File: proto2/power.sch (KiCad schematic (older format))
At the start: 24 parts, among them U13 LDO

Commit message: Fixing the issues the filter-fix merge created.
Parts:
- PS1: symbol BCR:CUI_PDQE20_ISOLATED_DCDC -> proto2-rescue:CUI_PDQE20_ISOLATED_DCDC-BCR
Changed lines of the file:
@@
 Raspberry Pi draws 1.3A and recomends 2.5A @ 5V.\nBeagleBone draws 1.2A and recomends at least 2A.
 $Comp
-L BCR:CUI_PDQE20_ISOLATED_DCDC PS1
+L proto2-rescue:CUI_PDQE20_ISOLATED_DCDC-BCR PS1
 U 1 1 61BF7DE1
 P 4050 2000
+AR Path="/61BF7DE1" Ref="PS1"  Part="1"
+AR Path="/619EB672/61BF7DE1" Ref="PS1"  Part="1"
 F 0 "PS1" H 4050 2425 50  0000 C CNN
 F 1 "CUI_PDQE20_ISOLATED_DCDC" H 4050 2334 50  0000 C CNN

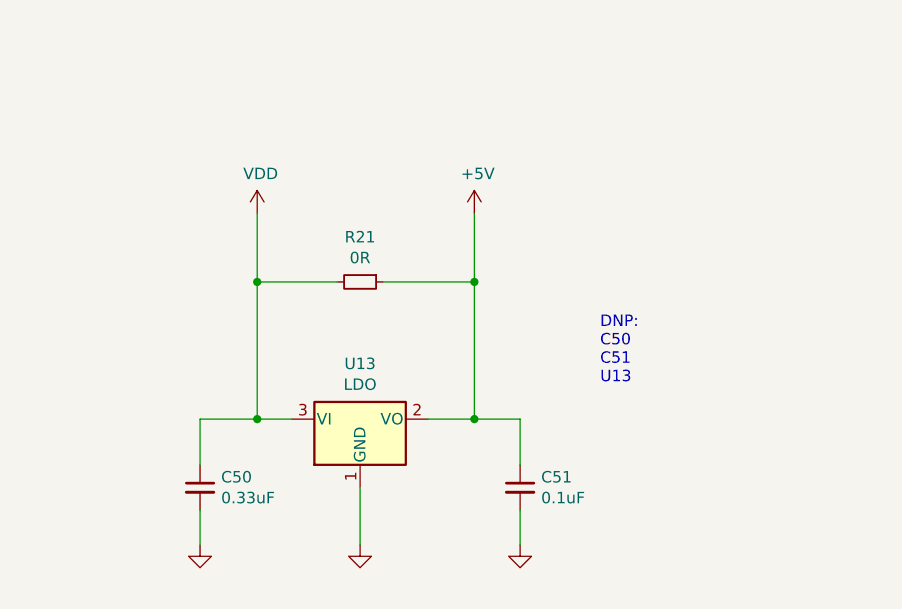
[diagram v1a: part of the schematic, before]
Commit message: Replaced LDO with a D2PAK type. Cleaned some traces.
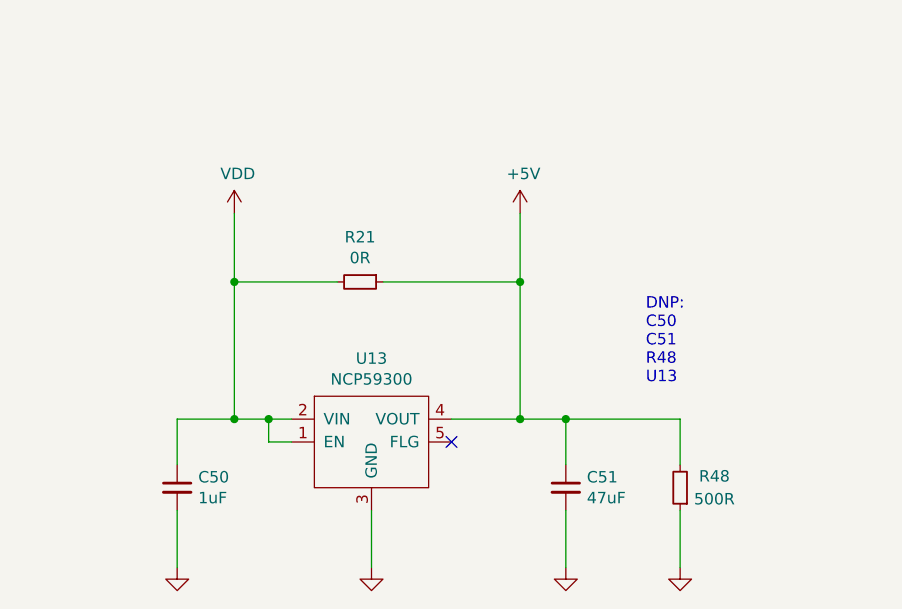
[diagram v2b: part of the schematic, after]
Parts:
- removed U13: LDO, JLCPCB:TO-252-2, symbol Regulator_Linear:AP1117-50
- added R48: 500R, Capacitor_SMD:C_0805_2012Metric, symbol Device:R_Small
- added U13: NCP59300, Package_TO_SOT_SMD:TO-263-5_TabPin3, symbol BCR:NCP59300
- C50: value 0.33uF -> 1uF; LCSC C1740 -> (none)
- C51: value 0.1uF -> 47uF; LCSC C49678 -> (none)
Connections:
- net +5V: now also R48.2, U13.4 (VOUT)
- net GND: now also R48.1, U13.3 (GND)
- net VDD: now also U13.1 (EN), U13.2 (VIN)
- no-connect marks 0 -> 1
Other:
- note added: "DNP:\nC50\nC51\nR48\nU13"
- note removed: "DNP:\nC50\nC51\nU13"
- moved on the sheet: C50, C51
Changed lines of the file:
@@
 Comment4 ""
 $EndDescr
-$Comp
-L Regulator_Linear:AP1117-50 U13
-U 1 1 61B47373
-P 3900 5500
-F 0 "U13" H 3900 5742 50  0000 C CNN
-F 1 "LDO" H 3900 5651 50  0000 C CNN
-F 2 "JLCPCB:TO-252-2" H 3900 5700 50  0001 C CNN
-F 3 "http://www.diodes.com/datasheets/AP1117.pdf" H 4000 5250 50  0001 C CNN
-F 4 "C58069" H 3900 5500 50  0001 C CNN "LCSC"
-	1    3900 5500
-	1    0    0    -1
-$EndComp
-Wire Wire Line
-	3900 5800 3900 6050
-Wire Wire Line
-	4200 5500 4400 5500
-Wire Wire Line
-	4400 5500 4400 4900
-Wire Wire Line
-	3600 5500 3450 5500
+Wire Wire Line
+	3950 5900 3950 6150
+Wire Wire Line
+	4300 5500 4600 5500
+Wire Wire Line
+	4600 5500 4600 4900
+Wire Wire Line
+	3600 5500 3500 5500
 Wire Wire Line
 	900  2200 900  2450
@@
 $EndComp
 Wire Wire Line
-	3450 5500 3450 4900
+	3350 5500 3350 4900
 $Comp
 L power:VDD #PWR0108
@@
 L power:VDD #PWR0109
 U 1 1 620C752B
-P 3450 4600
-F 0 "#PWR0109" H 3450 4450 50  0001 C CNN
-F 1 "VDD" H 3465 4773 50  0000 C CNN
-F 2 "" H 3450 4600 50  0001 C CNN
-F 3 "" H 3450 4600 50  0001 C CNN
-	1    3450 4600
+P 3350 4600
+F 0 "#PWR0109" H 3350 4450 50  0001 C CNN
+F 1 "VDD" H 3365 4773 50  0000 C CNN
+F 2 "" H 3350 4600 50  0001 C CNN
+F 3 "" H 3350 4600 50  0001 C CNN
+	1    3350 4600
 	1    0    0    -1
 $EndComp
@@
 L power:GND #PWR0112
 U 1 1 620C8052
-P 3900 6050
-F 0 "#PWR0112" H 3900 5800 50  0001 C CNN
-F 1 "GND" H 3905 5877 50  0001 C CNN
-F 2 "" H 3900 6050 50  0001 C CNN
-F 3 "" H 3900 6050 50  0001 C CNN
-	1    3900 6050
+P 3950 6150
+F 0 "#PWR0112" H 3950 5900 50  0001 C CNN
+F 1 "GND" H 3955 5977 50  0001 C CNN
+F 2 "" H 3950 6150 50  0001 C CNN
+F 3 "" H 3950 6150 50  0001 C CNN
+	1    3950 6150
 	1    0    0    -1
 $EndComp
@@
 $EndComp
 Wire Wire Line
-	3800 4900 3450 4900
-Connection ~ 3450 4900
-Wire Wire Line
-	3450 4900 3450 4600
-Wire Wire Line
-	4000 4900 4400 4900
-Connection ~ 4400 4900
-Wire Wire Line
-	4400 4900 4400 4600
+	3800 4900 3350 4900
+Connection ~ 3350 4900
+Wire Wire Line
+	3350 4900 3350 4600
+Wire Wire Line
+	4000 4900 4600 4900
+Connection ~ 4600 4900
+Wire Wire Line
+	4600 4900 4600 4600
 $Comp
 L Device:C_Small C50
 U 1 1 61BCD4E8
-P 3200 5800
-F 0 "C50" H 3292 5846 50  0000 L CNN
-F 1 "0.33uF" H 3292 5755 50  0000 L CNN
-F 2 "Capacitor_SMD:C_0805_2012Metric" H 3200 5800 50  0001 C CNN
-F 3 "~" H 3200 5800 50  0001 C CNN
-F 4 "C1740" H 3200 5800 50  0001 C CNN "LCSC"
-	1    3200 5800
+P 3100 5800
+F 0 "C50" H 3192 5846 50  0000 L CNN
+F 1 "1uF" H 3192 5755 50  0000 L CNN
+F 2 "Capacitor_SMD:C_0805_2012Metric" H 3100 5800 50  0001 C CNN
+F 3 "~" H 3100 5800 50  0001 C CNN
+F 4 "" H 3100 5800 50  0001 C CNN "LCSC"
+	1    3100 5800
 	1    0    0    -1
 $EndComp
@@
 L Device:C_Small C51
 U 1 1 61BCDFDB
-P 4600 5800
-F 0 "C51" H 4692 5846 50  0000 L CNN
-F 1 "0.1uF" H 4692 5755 50  0000 L CNN
-F 2 "Capacitor_SMD:C_0805_2012Metric" H 4600 5800 50  0001 C CNN
-F 3 "~" H 4600 5800 50  0001 C CNN
-F 4 "C49678" H 4600 5800 50  0001 C CNN "LCSC"
-	1    4600 5800
-	1    0    0    -1
-$EndComp
-Wire Wire Line
-	4400 5500 4600 5500
-Wire Wire Line
-	4600 5500 4600 5700
-Connection ~ 4400 5500
-Wire Wire Line
-	3450 5500 3200 5500
-Wire Wire Line
-	3200 5500 3200 5700
-Connection ~ 3450 5500
+P 4800 5800
+F 0 "C51" H 4892 5846 50  0000 L CNN
+F 1 "47uF" H 4892 5755 50  0000 L CNN
+F 2 "Capacitor_SMD:C_0805_2012Metric" H 4800 5800 50  0001 C CNN
+F 3 "~" H 4800 5800 50  0001 C CNN
+F 4 "" H 4800 5800 50  0001 C CNN "LCSC"
+	1    4800 5800
+	1    0    0    -1
+$EndComp
+Wire Wire Line
+	4600 5500 4800 5500
+Wire Wire Line
+	4800 5500 4800 5700
+Connection ~ 4600 5500
+Wire Wire Line
+	3350 5500 3100 5500
+Wire Wire Line
+	3100 5500 3100 5700
+Connection ~ 3350 5500
 $Comp
 L power:GND #PWR0122
 U 1 1 61BCFCA7
-P 3200 6050
-F 0 "#PWR0122" H 3200 5800 50  0001 C CNN
-F 1 "GND" H 3205 5877 50  0001 C CNN
-F 2 "" H 3200 6050 50  0001 C CNN
-F 3 "" H 3200 6050 50  0001 C CNN
-	1    3200 6050
+P 3100 6150
+F 0 "#PWR0122" H 3100 5900 50  0001 C CNN
+F 1 "GND" H 3105 5977 50  0001 C CNN
+F 2 "" H 3100 6150 50  0001 C CNN
+F 3 "" H 3100 6150 50  0001 C CNN
+	1    3100 6150
 	1    0    0    -1
 $EndComp
@@
 L power:GND #PWR0123
 U 1 1 61BCFF8F
-P 4600 6050
-F 0 "#PWR0123" H 4600 5800 50  0001 C CNN
-F 1 "GND" H 4605 5877 50  0001 C CNN
-F 2 "" H 4600 6050 50  0001 C CNN
-F 3 "" H 4600 6050 50  0001 C CNN
-	1    4600 6050
-	1    0    0    -1
-$EndComp
-Wire Wire Line
-	4600 6050 4600 5900
-Wire Wire Line
-	3200 6050 3200 5900
+P 4800 6150
+F 0 "#PWR0123" H 4800 5900 50  0001 C CNN
+F 1 "GND" H 4805 5977 50  0001 C CNN
+F 2 "" H 4800 6150 50  0001 C CNN
+F 3 "" H 4800 6150 50  0001 C CNN
+	1    4800 6150
+	1    0    0    -1
+$EndComp
+Wire Wire Line
+	4800 6150 4800 5900
+Wire Wire Line
+	3100 6150 3100 5900
 Wire Wire Line
 	1350 1900 1350 1800
@@
 Text Notes 9700 4750 0    50   ~ 0
 DNP:\nC52\nC53\nR18
-Text Notes 4950 5350 0    50   ~ 0
-DNP:\nC50\nC51\nU13
+Text Notes 5150 5350 0    50   ~ 0
+DNP:\nC50\nC51\nR48\nU13
 Text Notes 9150 2150 0    50   ~ 0
 DNP:\nR19\nR20
@@
 L power:+5V #PWR0104
 U 1 1 61DA9C72
-P 4400 4600
-F 0 "#PWR0104" H 4400 4450 50  0001 C CNN
-F 1 "+5V" H 4415 4773 50  0000 C CNN
-F 2 "" H 4400 4600 50  0001 C CNN
-F 3 "" H 4400 4600 50  0001 C CNN
-	1    4400 4600
+P 4600 4600
+F 0 "#PWR0104" H 4600 4450 50  0001 C CNN
+F 1 "+5V" H 4615 4773 50  0000 C CNN
+F 2 "" H 4600 4600 50  0001 C CNN
+F 3 "" H 4600 4600 50  0001 C CNN
+	1    4600 4600
 	1    0    0    -1
 $EndComp
@@
 	1    0    0    -1
 $EndComp
+$Comp
+L BCR:NCP59300 U13
+U 1 1 61CAD4D2
+P 3950 5800
+F 0 "U13" H 3950 6365 50  0000 C CNN
+F 1 "NCP59300" H 3950 6274 50  0000 C CNN
+F 2 "Package_TO_SOT_SMD:TO-263-5_TabPin3" H 3950 5800 50  0001 C CNN
+F 3 "https://www.onsemi.com/pdf/datasheet/ncp59300-d.pdf" H 3950 5800 50  0001 C CNN
+	1    3950 5800
+	1    0    0    -1
+$EndComp
+Wire Wire Line
+	3600 5600 3500 5600
+Wire Wire Line
+	3500 5600 3500 5500
+Connection ~ 3500 5500
+Wire Wire Line
+	3500 5500 3350 5500
+NoConn ~ 4300 5600
+$Comp
+L Device:R_Small R48
+U 1 1 61CC0990
+P 5300 5800
+F 0 "R48" H 5150 5750 50  0000 C CNN
+F 1 "500R" H 5150 5850 50  0000 C CNN
+F 2 "Capacitor_SMD:C_0805_2012Metric" H 5300 5800 50  0001 C CNN
+F 3 "~" H 5300 5800 50  0001 C CNN
+F 4 "C17888" H 5300 5800 50  0001 C CNN "LCSC"
+	1    5300 5800
+	-1   0    0    1
+$EndComp
+Wire Wire Line
+	5300 5700 5300 5500
+Wire Wire Line
+	5300 5500 4800 5500
+Connection ~ 4800 5500
+Wire Wire Line
+	5300 5900 5300 6150
+$Comp
+L power:GND #PWR013
+U 1 1 61CC641D
+P 5300 6150
+F 0 "#PWR013" H 5300 5900 50  0001 C CNN
+F 1 "GND" H 5305 5977 50  0001 C CNN
+F 2 "" H 5300 6150 50  0001 C CNN
+F 3 "" H 5300 6150 50  0001 C CNN
+	1    5300 6150
+	1    0    0    -1
+$EndComp

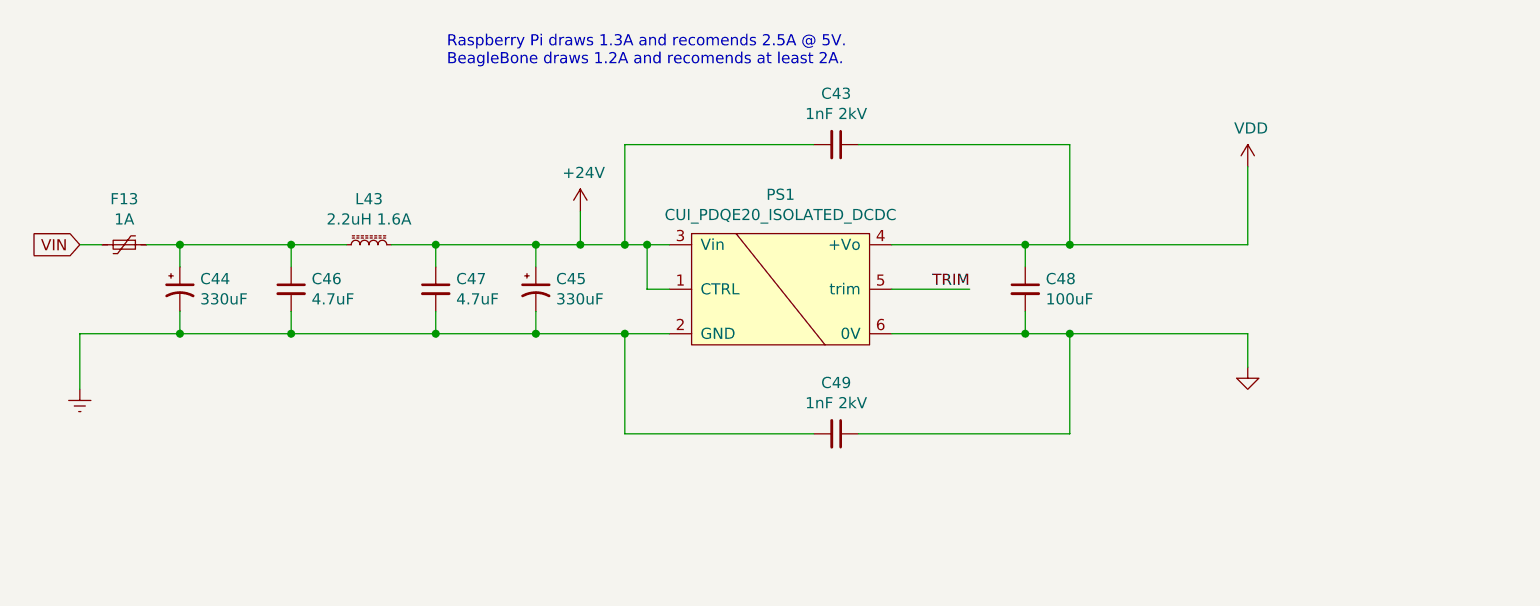
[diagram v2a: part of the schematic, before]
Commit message: Added reverse polarity diode.
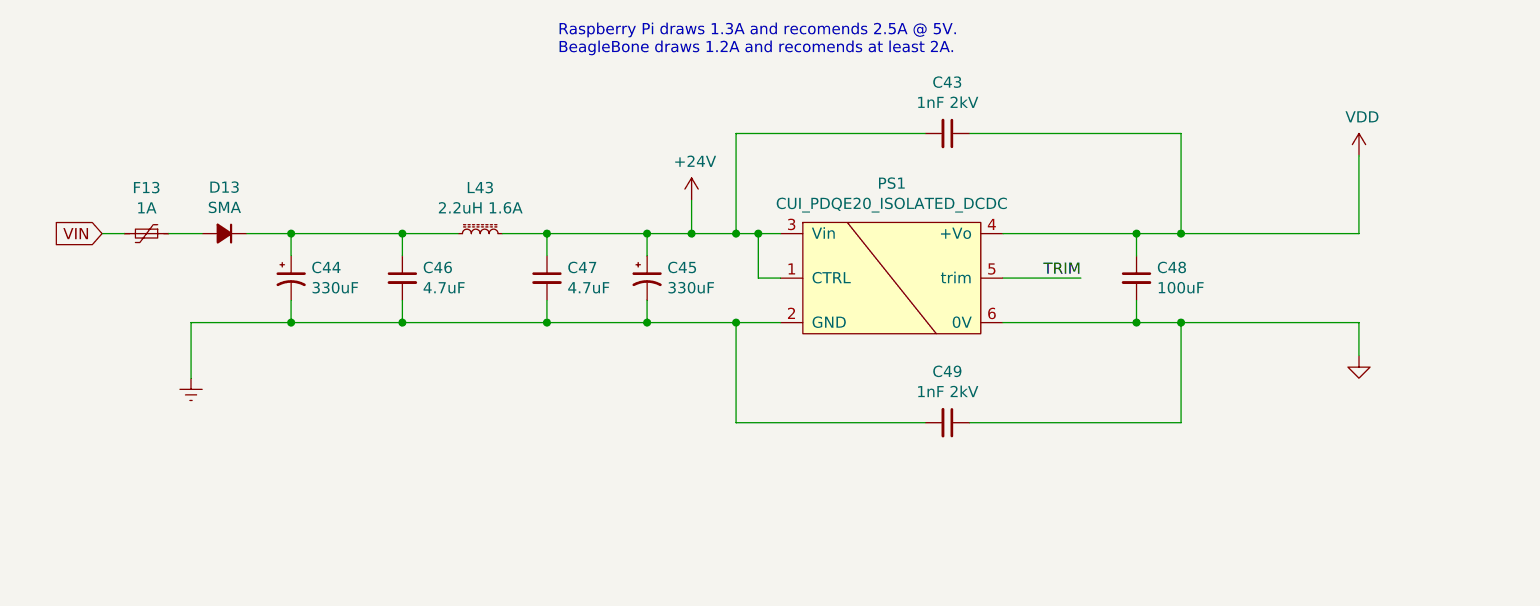
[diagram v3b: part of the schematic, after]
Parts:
- added D13: SMA, Diode_SMD:D_SOD-123F, symbol Device:D_Small_ALT
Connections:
- net at C44.1, C46.1, L43.1: now also D13.1 (K); no longer F13.1
- new net: D13.2 (A), F13.1
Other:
- moved on the sheet: C43, C44, C45, C46, C47, C48, C49, F13, L43, PS1

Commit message: Updates and changes for production run of 0.1.0
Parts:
- C52, C53: LCSC C49678 -> (none)
- R18: LCSC C17477 -> (none)
- R48: LCSC C17888 -> (none)
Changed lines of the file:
@@
 F 2 "Resistor_SMD:R_0805_2012Metric" H 9250 4500 50  0001 C CNN
 F 3 "~" H 9250 4500 50  0001 C CNN
-F 4 "C17477" H 9250 4500 50  0001 C CNN "LCSC"
+F 4 "" H 9250 4500 50  0001 C CNN "LCSC"
 	1    9250 4500
 	0    1    1    0
@@
 F 2 "Capacitor_SMD:C_0805_2012Metric" H 8750 4850 50  0001 C CNN
 F 3 "~" H 8750 4850 50  0001 C CNN
-F 4 "C49678" H 8750 4850 50  0001 C CNN "LCSC"
+F 4 "" H 8750 4850 50  0001 C CNN "LCSC"
 	1    8750 4850
 	0    1    1    0
@@
 F 2 "Capacitor_SMD:C_0805_2012Metric" H 9250 4850 50  0001 C CNN
 F 3 "~" H 9250 4850 50  0001 C CNN
-F 4 "C49678" H 9250 4850 50  0001 C CNN "LCSC"
+F 4 "" H 9250 4850 50  0001 C CNN "LCSC"
 	1    9250 4850
 	0    1    1    0
@@
 F 2 "Capacitor_SMD:C_0805_2012Metric" H 5300 5800 50  0001 C CNN
 F 3 "~" H 5300 5800 50  0001 C CNN
-F 4 "C17888" H 5300 5800 50  0001 C CNN "LCSC"
+F 4 "" H 5300 5800 50  0001 C CNN "LCSC"
 	1    5300 5800
 	-1   0    0    1
